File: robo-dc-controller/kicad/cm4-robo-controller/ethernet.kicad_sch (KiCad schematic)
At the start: 6 parts, among them U7 TPD4EUSB30DQAR, U8 TPD4EUSB30DQAR

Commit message: Latest ethernet changes
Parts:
- removed R16, R17: 1.5kΩ, PCM_JLCPCB:R_0402, symbol PCM_JLCPCB-Resistors:0402,1.5kΩ
- added R16, R17: 470Ω, PCM_JLCPCB:R_0402, symbol PCM_JLCPCB-Resistors:0402,470Ω
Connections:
- net ETH_LEDG: now also R16.1
- net ETH_LEDY: now also R17.2
- net at RJ1.16: now also R16.2
- net at RJ1.18: now also R17.1
- net 5V renamed 3V3_CM4
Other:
- note added: "CM4 Ethernet_nLED pins are active-low 3.3V sinks, IOL 8mA @ VOL 0.4V. ETH_LEDG = activity (green), ETH_LEDY = link speed (yellow). RJ1 pins 15/17 are the LED anodes."
- note added: "Clamps all four pairs on the CM4 side of the magnetics. Place both at RJ1."
- note added: "Ethernet ESD"
- note added: "Gigabit Ethernet - CM4 MDI to RJ45"
- note added: "LED pin connections from datasheet"
- note added: "LPJG0926HENL, shielded, LEDs, PoE-capable (LCSC C22457393). EP0-EP3 come straight from the CM4 - the PHY is on the module, no external PHY. TD center taps (pins 4, 5) bypassed to GND by C17 100nF. VC1-VC4 (pins 11-14) are the cable-side PoE taps - unused, no PoE on this board. Shield (pins 19, 20) tied to signal GND."
- note added: "RJ45 with integrated magnetics"
- note added: "Route EP0-EP3 as 100R differential pairs, matched within 0.15mm. Keep the RJ1 chassis/shield area clear of the signal ground pour."
- moved on the sheet: C17, RJ1, U7, U8

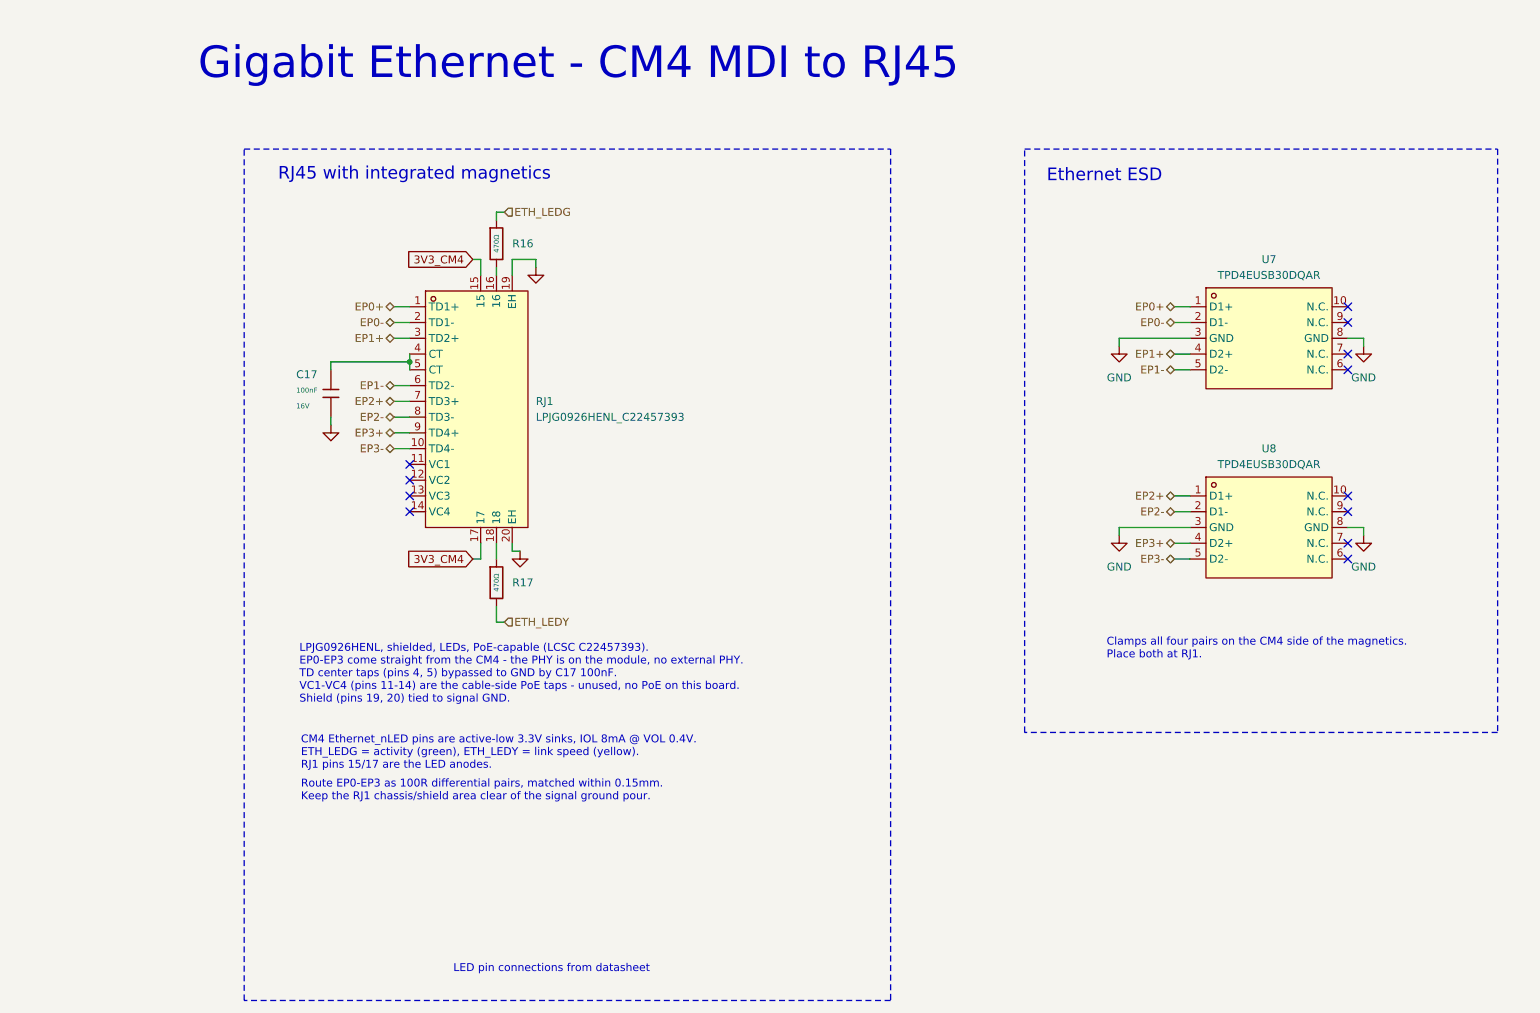
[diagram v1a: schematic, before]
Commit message: Opdated to HR911130A
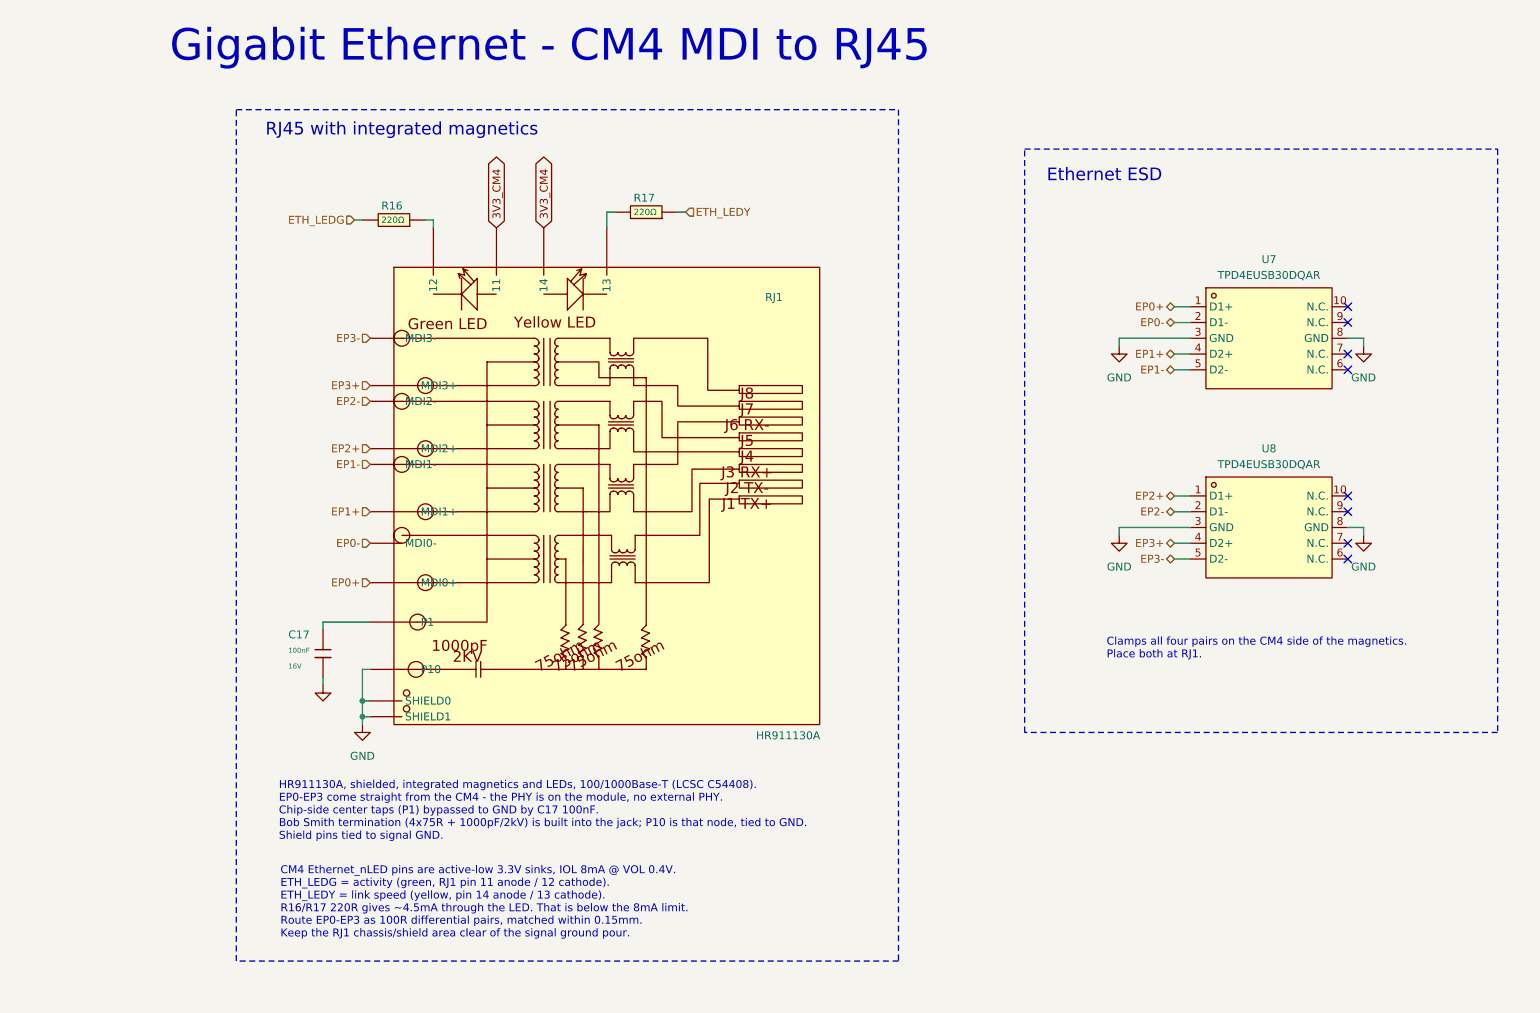
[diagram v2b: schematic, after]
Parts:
- removed R16, R17: 470Ω, PCM_JLCPCB:R_0402, symbol PCM_JLCPCB-Resistors:0402,470Ω
- removed RJ1: LPJG0926HENL_C22457393, MyParts:RJ45-TH_LPJG0926HENL_C22457393, symbol MyParts:LPJG0926HENL_C22457393
- added R16, R17: 220Ω, MyParts:R0402, symbol MyParts:0402WGF2200TCE
- added RJ1: HR911130A, MyParts:RJ45-TH_HR911130A, symbol MyParts:HR911130A
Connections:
- net 3V3_CM4: now also RJ1.11, RJ1.14
- net EP0+: now also RJ1.P2 (MDI0+)
- net EP0-: now also RJ1.P3 (MDI0-)
- net EP1+: now also RJ1.P4 (MDI1+)
- net EP1-: now also RJ1.P7 (MDI1-)
- net EP2+: now also RJ1.P5 (MDI2+)
- net EP2-: now also RJ1.P6 (MDI2-)
- net EP3+: now also RJ1.P8 (MDI3+)
- net EP3-: now also RJ1.P9 (MDI3-)
- net ETH_LEDG: now also R16.2
- net ETH_LEDY: now also R17.1
- net GND: now also RJ1.P10, RJ1.SHIELD0, RJ1.SHIELD1
- net at C17.1: now also RJ1.P1
- new net: R17.2, RJ1.13
- new net: R16.1, RJ1.12
- no-connect marks 12 -> 8
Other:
- note added: "CM4 Ethernet_nLED pins are active-low 3.3V sinks, IOL 8mA @ VOL 0.4V. ETH_LEDG = activity (green, RJ1 pin 11 anode / 12 cathode). ETH_LEDY = link speed (yellow, pin 14 anode / 13 cathode). R16/R17 220R gives ~4.5mA through the LED. That is below the 8mA limit."
- note added: "HR911130A, shielded, integrated magnetics and LEDs, 100/1000Base-T (LCSC C54408). EP0-EP3 come straight from the CM4 - the PHY is on the module, no external PHY. Chip-side center taps (P1) bypassed to GND by C17 100nF. Bob Smith termination (4x75R + 1000pF/2kV) is built into the jack; P10 is that node, tied to GND. Shield pins tied to signal GND."
- note removed: "CM4 Ethernet_nLED pins are active-low 3.3V sinks, IOL 8mA @ VOL 0.4V. ETH_LEDG = activity (green), ETH_LEDY = link speed (yellow). RJ1 pins 15/17 are the LED anodes."
- note removed: "LED pin connections from datasheet"
- note removed: "LPJG0926HENL, shielded, LEDs, PoE-capable (LCSC C22457393). EP0-EP3 come straight from the CM4 - the PHY is on the module, no external PHY. TD center taps (pins 4, 5) bypassed to GND by C17 100nF. VC1-VC4 (pins 11-14) are the cable-side PoE taps - unused, no PoE on this board. Shield (pins 19, 20) tied to signal GND."
- moved on the sheet: C17

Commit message: CM4 carrier: GPS sheet integration, U12 expansion header, power fixes
Populate U12 (2x12 expansion header) on the CM4_Connectors sheet:
all 19 CM4 signals plus 3V3_CM4 and four grounds, with 2.2k I2C
pull-ups (R113/R114) on GPIO2/GPIO3. Value matches the CM4IO
reference design, which uses 2.2k on SDA1/SCL1.

Wire the new GPS sheet (MAX-M10S) into the CM4 sheet: add sheet pins
for GPS_RX_MCU, GPS_TX_MCU and 1PPS_MCU. The UART lands on UART3
(GPIO4 = TXD3 to the GPS RXD, GPIO5 = RXD3 from the GPS TXD) and
1PPS on GPIO16. Needs dtoverlay=uart3 in config.txt. The leftover
CM4_TX/CM4_RX/1PPS_MCU hierarchical labels, which pointed at a root
sheet with no matching pins, become local labels on those nets.

Fix the orphaned 3V3 label on the GPS sheet, which left the MS621FE
backup cell with no charge path, and scope 3V3_CM4 to the CM4
hierarchy: local labels in the CM4 sheet, hierarchical labels plus
sheet pins in each consuming sub-sheet. Net membership is unchanged
at 30 nodes.

Add PWR_FLAGs on the 5V rail and on GND. Both are driven through
passive parts (an inductor and ground symbols respectively), so ERC
could not see a driver.

ERC: 55 -> 40 violations. Of the remainder, 30 are the RoboClaw U1,
which is placed on the root sheet but not yet wired.
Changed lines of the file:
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@@
 		)
 	)
-	(global_label "3V3_CM4"
-		(shape bidirectional)
+	(hierarchical_label "3V3_CM4"
+		(shape input)
 		(at 86.36 48.26 90)
 		(effects
@@
 			(justify left)
 		)
-		(property "Intersheetrefs" "${INTERSHEET_REFS}"
-			(at 86.36 48.26 0)
-			(hide yes)
-			(show_name no)
-			(do_not_autoplace no)
-			(effects
-				(font
-					(size 1.27 1.27)
-				)
-			)
-		)
 	)
-	(global_label "3V3_CM4"
-		(shape bidirectional)
+	(hierarchical_label "3V3_CM4"
+		(shape input)
 		(at 78.74 48.26 90)
 		(effects
@@
 			(justify left)
 		)
-		(property "Intersheetrefs" "${INTERSHEET_REFS}"
-			(at 78.74 48.26 0)
-			(hide yes)
-			(show_name no)
-			(do_not_autoplace no)
-			(effects
-				(font
-					(size 1.27 1.27)
-				)
-			)
-		)
 	)
